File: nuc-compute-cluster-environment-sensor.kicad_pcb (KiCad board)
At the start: 4 copper layers, 50 x 26.5 mm, 118 parts, among them J1 USB4105-GF-A, J2 SM04B-SRSS-TB-LF-SN, J3 SM04B-SRSS-TB-LF-SN, U1 FT4232H-56Q, U2 AP7370-33SA-7, U3 STM32G474CET6, U4 MB85RC1MTPNF-G, U5 SHT45, U6 BME280, Y1 ABM3B-12.000MHZ-B2-T, Y2 ECS-_327-12_5-34B-TR, Y3 ABM3B-8.000MHZ-10-1-U-T

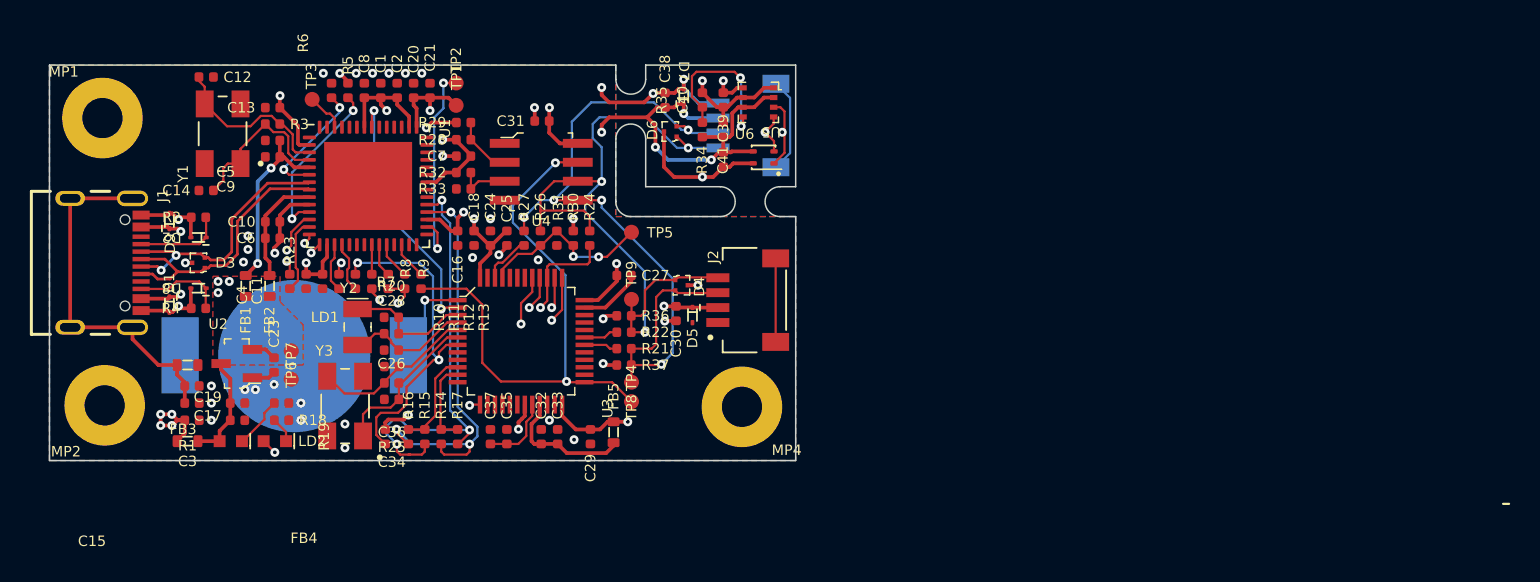
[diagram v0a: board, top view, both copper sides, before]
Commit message: Designators' placement finished, DRC performed with no issues found
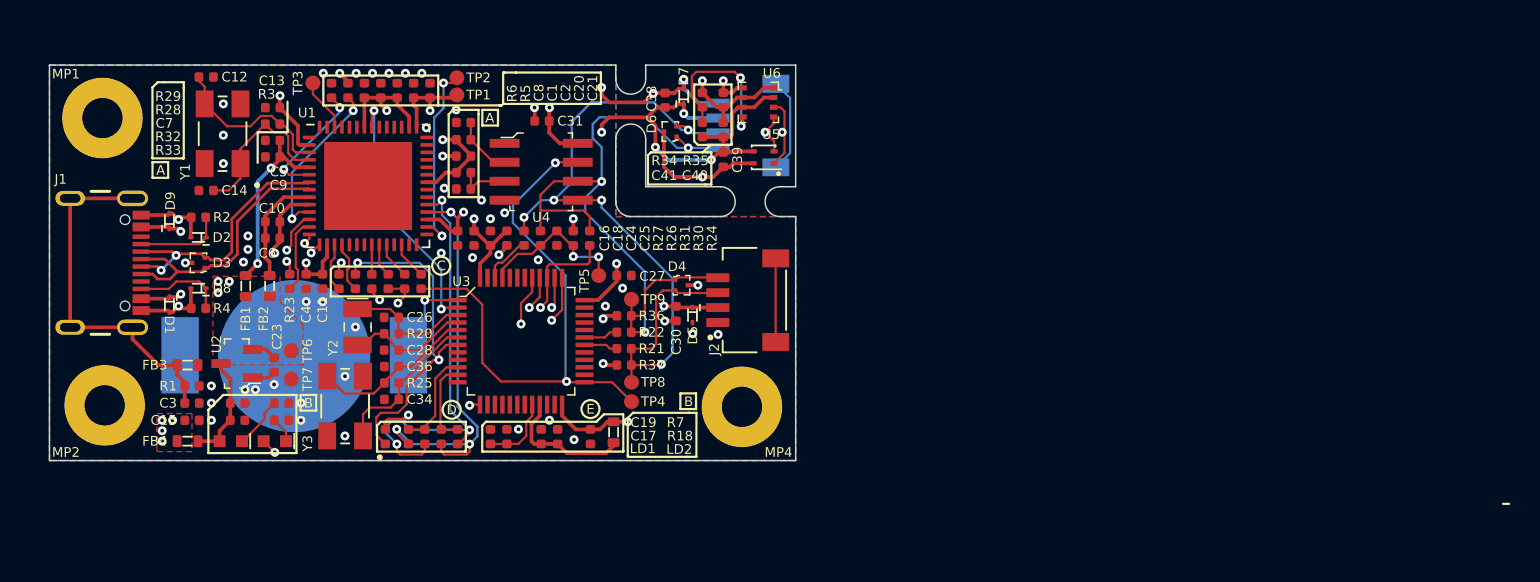
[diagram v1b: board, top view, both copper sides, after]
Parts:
- moved TP5 3.64 mm to (196.8, 127.6)
- moved TP3 1.10 mm to (177.7, 114.7)
- moved TP1 0.70 mm to (187.3, 115.5)
- moved TP2 0.35 mm to (187.3, 114.3)
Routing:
- net GND: track 66.8 -> 58.5 mm, vias 40 -> 55
- net /VBUS: track 11.5 -> 5.57 mm
- net Net-(R26-Pad1): track 12.1 -> 10.5 mm
- net Net-(TP2-Pad1): track 14.2 -> 13.0 mm
- net Net-(TP3-Pad1): track 2.63 -> 3.56 mm
- added copper zone on F.Cu, net /VBUS
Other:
- outline, holes or cut-outs redrawn
- board text added: "A"
- board text added: "B"
- board text added: "C"
- board text added: "D"
- board text added: "E"

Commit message: Added 1k pullup on FRAM write protection pin, 470R serial resistors added on SWDIO and SWCLK, keepout zones for GND added around USB
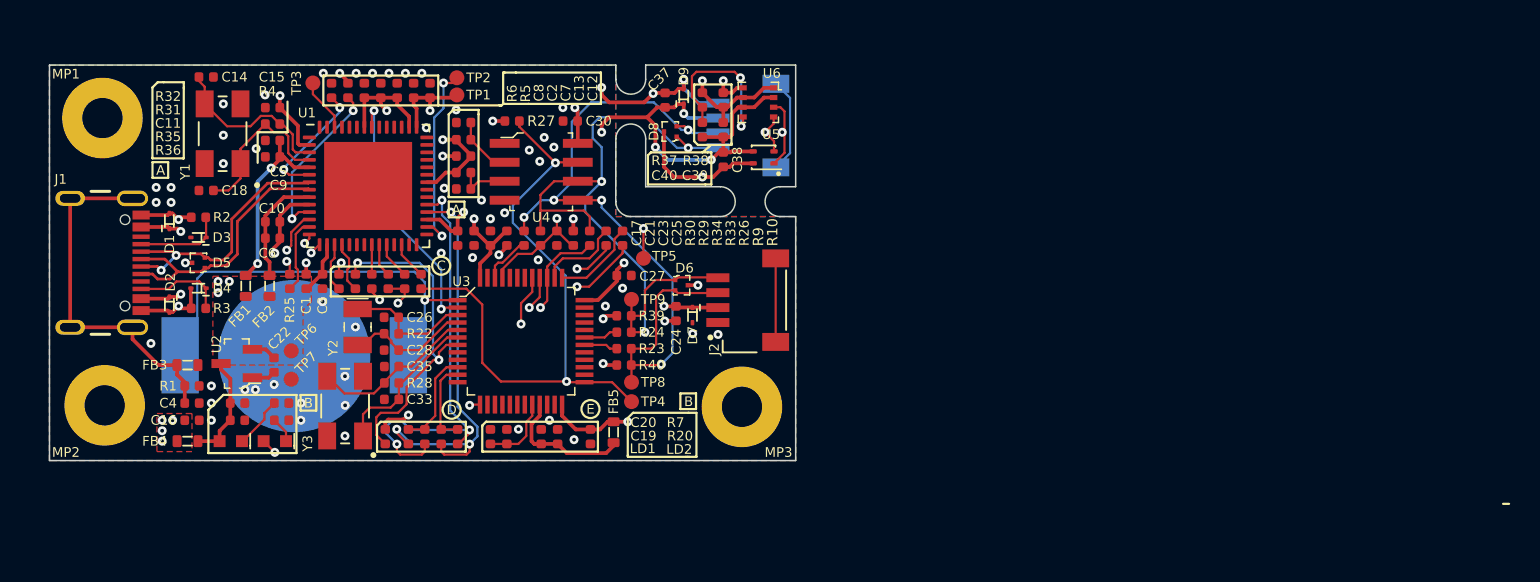
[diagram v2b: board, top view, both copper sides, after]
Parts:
- added R10: R_470R_0402, antmicro-footprints:0402-res, F.Cu at (198.4, 125.1)
- added R27: R_1k_0402, antmicro-footprints:0402-res, F.Cu at (191.0, 117.2)
- added R9: R_470R_0402, antmicro-footprints:0402-res, F.Cu at (197.3, 125.1)
- moved TP5 3.21 mm to (199.8, 126.5)
- moved C30 1.90 mm to (194.9, 117.2)
- turned C1 to 90 degrees
- renumbered C4 to C1, C7 to C11, C21 to C12, C20 to C13, C12 to C14, C13 to C15, C15 to C16, C16 to C17, C14 to C18, C17 to C19, C1 to C2, C19 to C20, C18 to C21, C23 to C22, C24 to C23, C30 to C24, C11 to C3, C31 to C30, C32 to C31, C33 to C32, C34 to C33, C35 to C34, C36 to C35, C37 to C36, C38 to C37, C39 to C38, C40 to C39, C3 to C4, C41 to C40, C2 to C7, D9 to D1, D1 to D2, D2 to D3, D8 to D4, D3 to D5, D4 to D6, D5 to D7, D6 to D8, D7 to D9, MP4 to MP3, R9 to R11, R10 to R12, R11 to R13, R12 to R14, R13 to R15, R14 to R16, R15 to R17, R16 to R18, R17 to R19, R18 to R20, R19 to R21, R20 to R22, R21 to R23, R22 to R24, R23 to R25, R24 to R26, R25 to R28, R26 to R29, R4 to R3, R27 to R30, R28 to R31, R29 to R32, R30 to R33, R31 to R34, R32 to R35, R33 to R36, R34 to R37, R35 to R38, R36 to R39, R3 to R4, R37 to R40
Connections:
- U1 pad 12: SWCLK-JTCK -> Net-(U1-Pad12)
- U1 pad 15: SWDIO-JTMS -> Net-(U1-Pad15)
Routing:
- net Net-(U1-Pad12): track 0.00 -> 28.8 mm, vias 0 -> 2
- net Net-(U1-Pad15): track 0.00 -> 26.1 mm, vias 0 -> 2
- net Net-(BAT1-PadP): track 6.36 -> 28.9 mm
- net SWCLK-JTCK: track 26.1 -> 5.61 mm, vias 2 -> 0
- net SWDIO-JTMS: track 22.3 -> 5.77 mm, vias 2 -> 0
- net Net-(R29-Pad1): track 10.5 -> 15.7 mm
- net /FRAM_WP: track 38.4 -> 42.2 mm
- net GND: track 58.5 -> 57.0 mm, vias 55 -> 64
- net +3V3: track 83.5 -> 82.7 mm
- net Net-(R25-Pad2): track 28.7 -> 28.0 mm

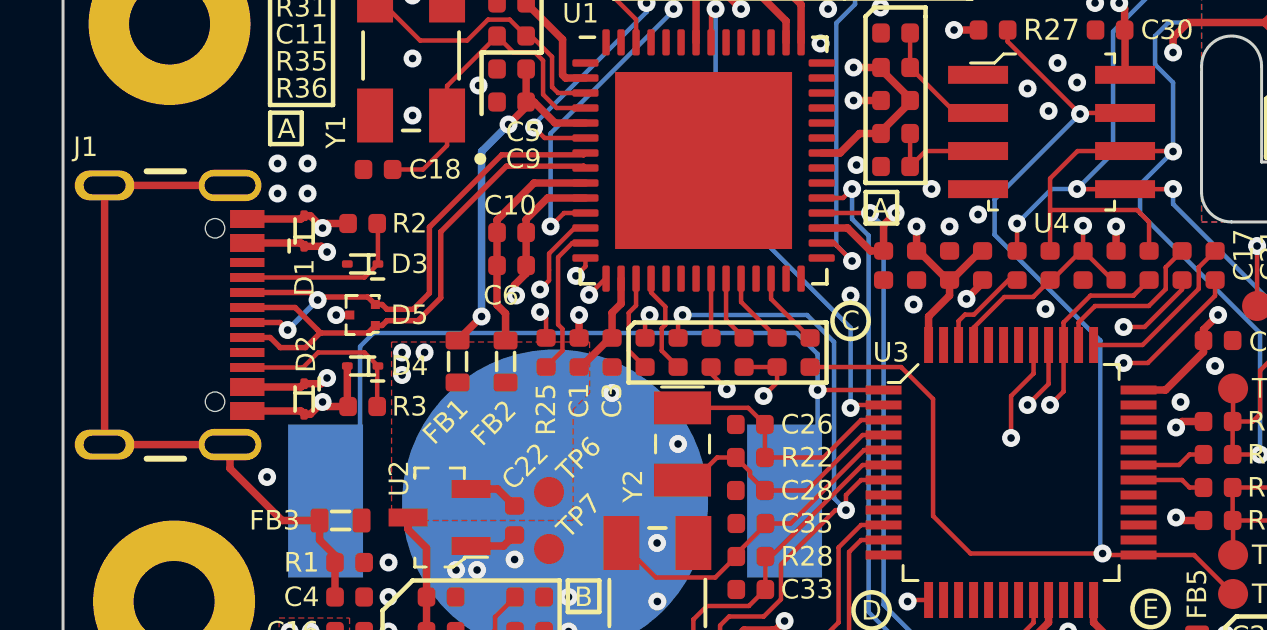
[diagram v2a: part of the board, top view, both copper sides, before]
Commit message: Clearance on filled zones increased to 0,25mm, small tweaks added on layout
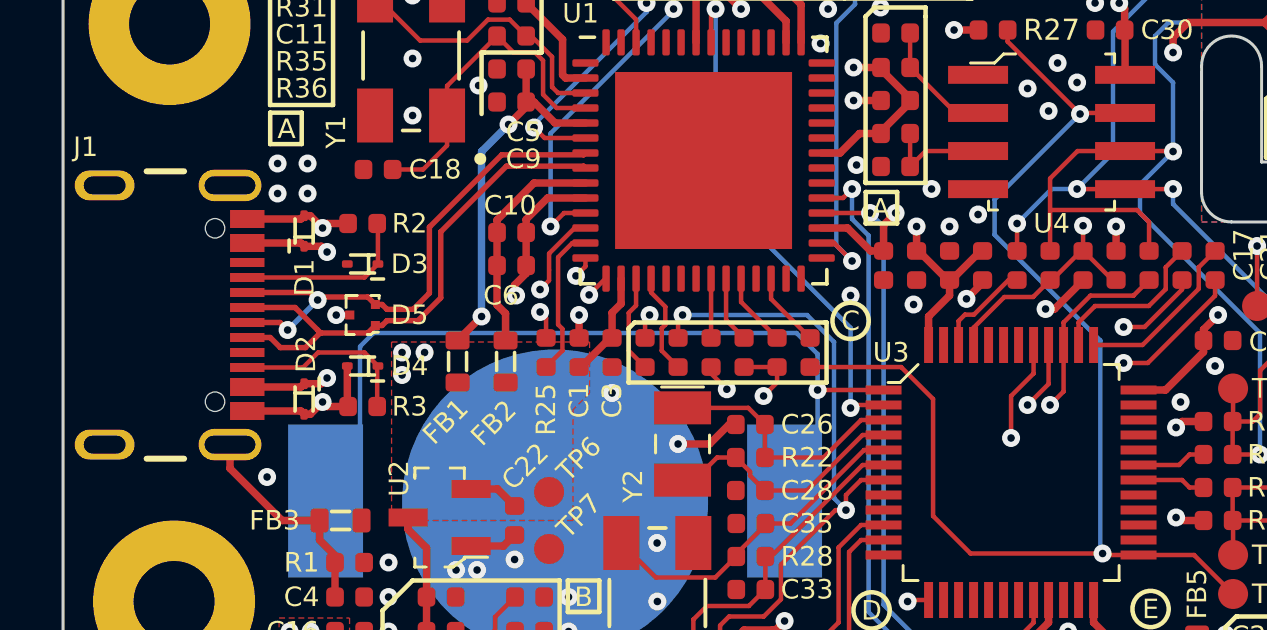
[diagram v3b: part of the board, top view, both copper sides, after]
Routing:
- net GND: track 57.0 -> 60.8 mm
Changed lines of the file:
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@@
   (segment (start 204.47 121) (end 205.15 120.32) (width 0.25) (layer "F.Cu") (net 1))
   (segment (start 173.6 134.45) (end 174.685 134.45) (width 0.25) (layer "F.Cu") (net 1))
+  (segment (start 182.425 130.4) (end 182.2 130.4) (width 0.25) (layer "F.Cu") (net 1))
+  (segment (start 181.55 131.05) (end 180.5 131.05) (width 0.25) (layer "F.Cu") (net 1))
   (segment (start 169.475 129.775) (end 169.5 129.8) (width 0.25) (layer "F.Cu") (net 1))
   (segment (start 168.035 130.06) (end 168.24 130.06) (width 0.25) (layer "F.Cu") (net 1))
@@
   (segment (start 200.485 115.365) (end 200.45 115.4) (width 0.25) (layer "F.Cu") (net 1))
   (segment (start 203.75 121) (end 204.47 121) (width 0.25) (layer "F.Cu") (net 1))
+  (segment (start 193.05 126.55) (end 192.75 126.55) (width 0.25) (layer "F.Cu") (net 1))
   (segment (start 204.72 116.32) (end 203.75 115.35) (width 0.25) (layer "F.Cu") (net 1))
+  (segment (start 194 125.585) (end 194 125.6) (width 0.25) (layer "F.Cu") (net 1))
   (segment (start 168.035 123.44) (end 168.24 123.44) (width 0.25) (layer "F.Cu") (net 1))
   (segment (start 201.25 115.365) (end 200.485 115.365) (width 0.25) (layer "F.Cu") (net 1))
+  (segment (start 194 125.6) (end 193.05 126.55) (width 0.25) (layer "F.Cu") (net 1))
   (segment (start 175.435 125.1) (end 175.435 125.365) (width 0.25) (layer "F.Cu") (net 1))
   (segment (start 202.16 115.09) (end 201.885 115.365) (width 0.25) (layer "F.Cu") (net 1))
@@
   (segment (start 190.65 125.585) (end 190.65 125.676014) (width 0.25) (layer "F.Cu") (net 1))
   (segment (start 177.2 127.515) (end 177.2 126.75) (width 0.25) (layer "F.Cu") (net 1))
+  (segment (start 182.2 130.4) (end 181.55 131.05) (width 0.25) (layer "F.Cu") (net 1))
   (via (at 177.2 126.75) (size 0.6) (drill 0.25) (layers "F.Cu" "B.Cu") (net 1))
   (via (at 186.45 121.75) (size 0.6) (drill 0.25) (layers "F.Cu" "B.Cu") (net 1))
@@
   (segment (start 167.3 133.6) (end 168.55 133.6) (width 0.25) (layer "F.Cu") (net 4))
   (segment (start 168.55 134.25) (end 168.55 133.6) (width 0.25) (layer "F.Cu") (net 4))
-  (segment (start 165.565 131.07) (end 161.385 131.07) (width 0.25) (layer "F.Cu") (net 4))
-  (segment (start 161.385 122.43) (end 165.565 122.43) (width 0.25) (layer "F.Cu") (net 4))
-  (segment (start 161.385 131.07) (end 161.385 122.43) (width 0.25) (layer "F.Cu") (net 4))
   (segment (start 169.065 135) (end 169.065 134.765) (width 0.25) (layer "F.Cu") (net 4))
+  (segment (start 161.385 122.43) (end 161.385 131.07) (width 0.25) (layer "In2.Cu") (net 4))
+  (segment (start 161.385 131.07) (end 165.565 131.07) (width 0.25) (layer "In2.Cu") (net 4))
+  (segment (start 165.565 122.43) (end 161.385 122.43) (width 0.25) (layer "In2.Cu") (net 4))
   (segment (start 175.435 119.65) (end 175.435 118.55) (width 0.25) (layer "F.Cu") (net 5))
   (segment (start 173.15 127.6) (end 173.95 126.8) (width 0.25) (layer "F.Cu") (net 5))
@@
   )
   (zone (net 1) (net_name "GND") (layers "F.Cu" "In1.Cu" "B.Cu") (name "GND") (hatch edge 0.508)
-    (connect_pads (clearance 0.15))
+    (connect_pads (clearance 0.25))
     (min_thickness 0.15) (filled_areas_thickness no)
     (fill yes (thermal_gap 0.15) (thermal_bridge_width 0.25))
@@
   )
   (zone (net 3) (net_name "+3V3") (layer "In2.Cu") (name "+3V3") (hatch edge 0.508)
-    (connect_pads (clearance 0.15))
+    (connect_pads (clearance 0.25))
     (min_thickness 0.15) (filled_areas_thickness no)
     (fill yes (thermal_gap 0.15) (thermal_bridge_width 0.25))
@@
   )
   (zone (net 10) (net_name "/VBUS") (layer "In2.Cu") (name "USB_VBUS") (hatch edge 0.508)
-    (connect_pads (clearance 0.15))
+    (connect_pads (clearance 0.25))
     (min_thickness 0.15) (filled_areas_thickness no)
     (fill yes (thermal_gap 0.15) (thermal_bridge_width 0.25))

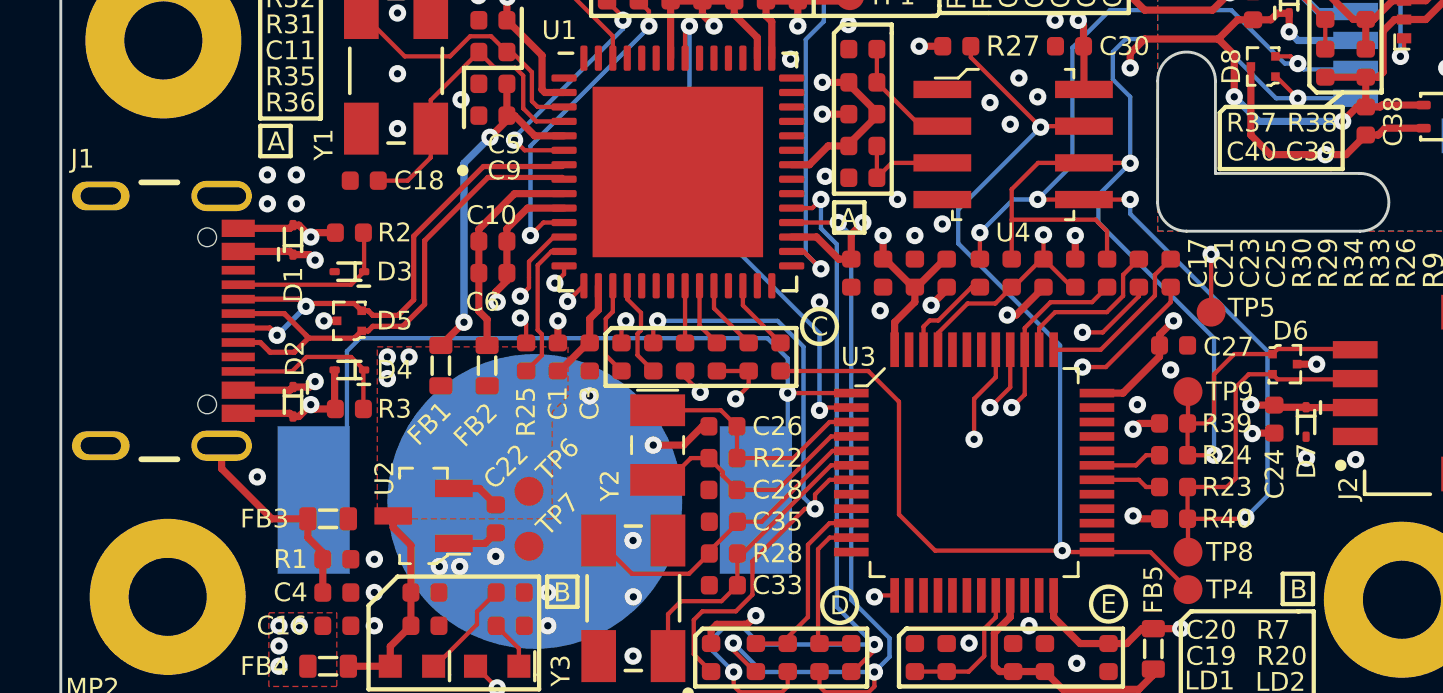
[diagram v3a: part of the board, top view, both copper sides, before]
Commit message: Added board markings, Rev 1.0.1
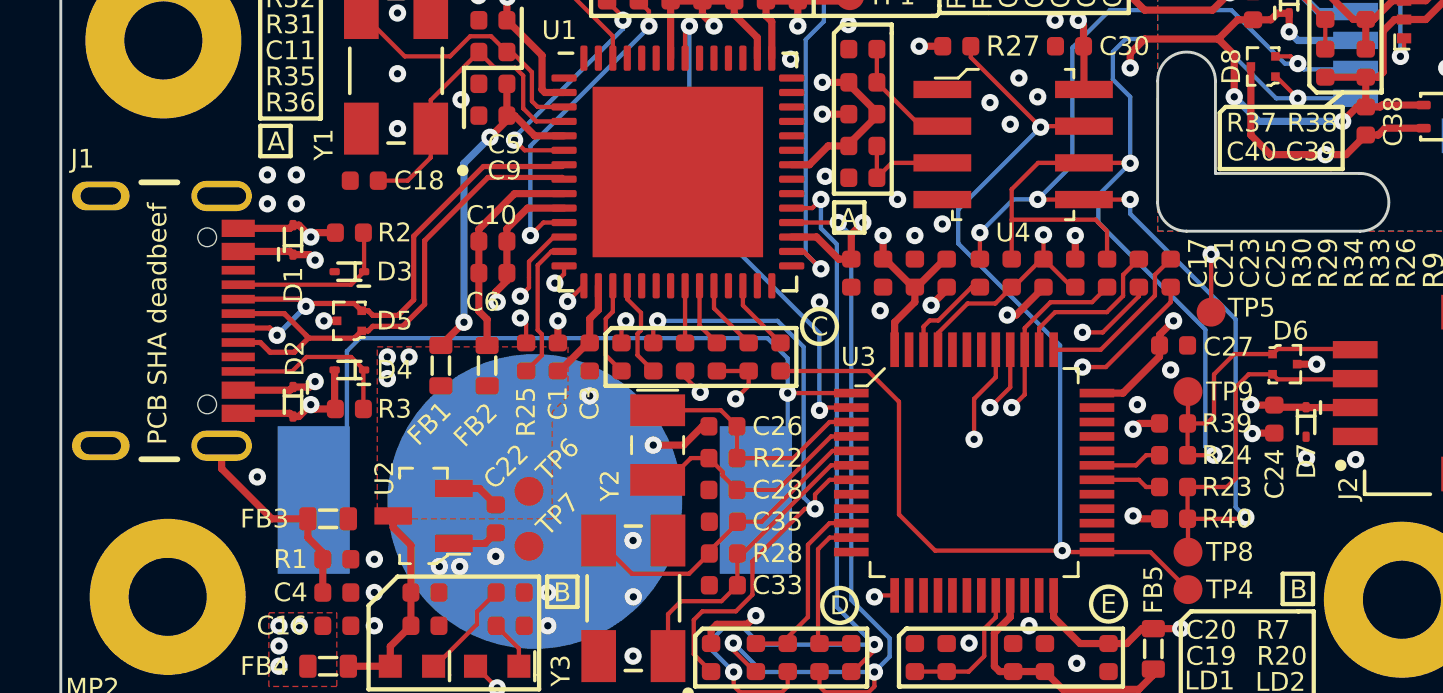
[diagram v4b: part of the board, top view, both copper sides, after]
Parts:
- added G***: LOGO, antmicro-footprints:antmicro-logo_scaled_12mm_mask, B.Cu at (170.2, 120.0)
- added REF**: OSHW-Logo_7.5x8mm_Mask, antmicro-footprints:OSHW-Logo_7.5x8mm_Mask, B.Cu at (205.2, 128.4)
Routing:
- net I2C_1_SDA: track 84.7 -> 84.0 mm
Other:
- board text added: "Environment Sensor"
- board text added: "PCB SHA deadbeef"
- board text added: "Rev. 1.0.1 01/2022"
